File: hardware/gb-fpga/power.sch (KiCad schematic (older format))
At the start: 39 parts, among them J3 BAT+, J4 BAT-, Q1 MBT3904DW1, SW1 Switch, U4 LTC3555, U5 TLV61046ADB

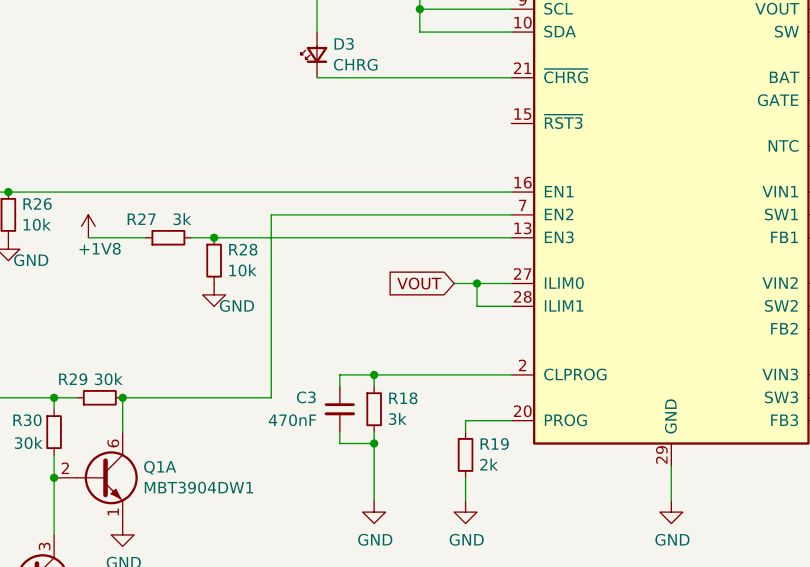
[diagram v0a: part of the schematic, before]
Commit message: Fix connection on U4
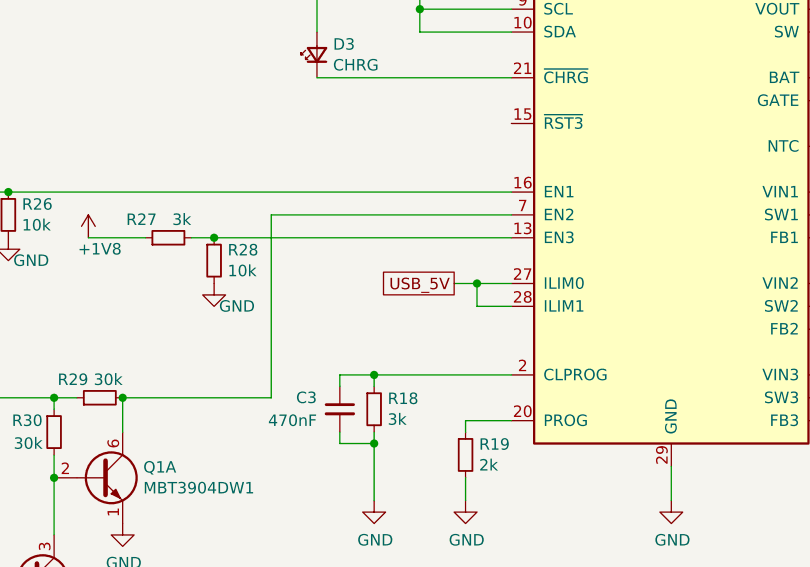
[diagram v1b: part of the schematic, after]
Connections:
- net USB_5V: now also U4.27 (ILIM0), U4.28 (ILIM1)
- net VOUT: no longer U4.27 (ILIM0), U4.28 (ILIM1)
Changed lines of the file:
@@
 	5500 3400 5500 3600
 Connection ~ 5500 3600
-Text GLabel 3550 4000 0    50   Input ~ 0
-VOUT
 Wire Wire Line
 	3550 4000 3650 4000
@@
 	1    0    0    -1
 $EndComp
+Text GLabel 3550 4000 0    50   UnSpc ~ 0
+USB_5V
 $EndSCHEMATC
